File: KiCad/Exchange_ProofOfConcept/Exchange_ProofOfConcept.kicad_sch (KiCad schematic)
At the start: 25 parts, among them J1 Conn_02x03_Odd_Even, J2 Conn_02x03_Odd_Even, J3 Conn_01x04, J7 Screw_Terminal_01x02, J9 Screw_Terminal_01x08, U1 MCP23017, U2 MCP23017, U3 MT8816

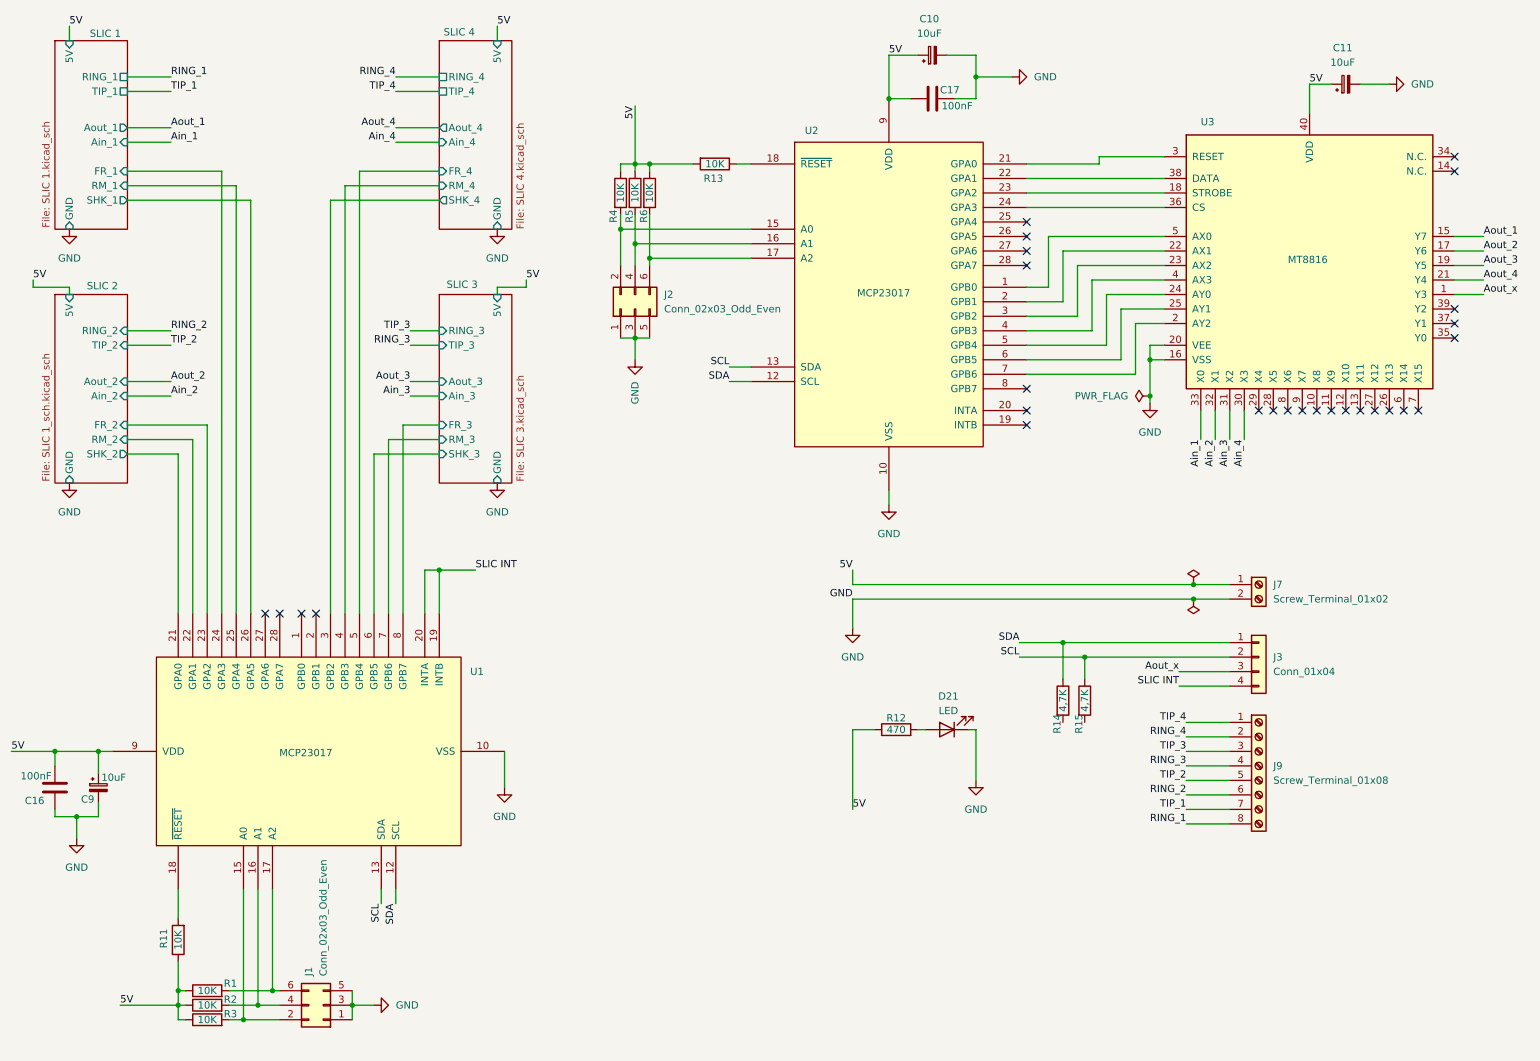
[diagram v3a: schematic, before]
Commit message: deleted:    KiCad/Exchange_ProofOfConcept/Exchange_ProofOfConcept-backups/Exchange_ProofOfConcept-2024-09-22_005800.zip 	deleted:    KiCad/Exchange_ProofOfConcept/Exchange_ProofOfConcept-backups/Exchange_ProofOfConcept-2024-09-22_010415.zip 	deleted:    KiCad/Exchange_ProofOfConcept/Exchange_ProofOfConcept-backups/Exchange_ProofOfConcept-2024-09-22_093037.zip 	deleted:    KiCad/Exchange_ProofOfConcept/Exchange_ProofOfConcept-backups/Exchange_ProofOfConcept-2024-09-22_093847.zip 	deleted:    KiCad/Exchange_ProofOfConcept/Exchange_ProofOfConcept-backups/Exchange_ProofOfConcept-2024-09-22_094927.zip 	deleted:    KiCad/Exchange_ProofOfConcept/Exchange_ProofOfConcept-backups/Exchange_ProofOfConcept-2024-10-02_184119.zip 	deleted:    KiCad/Exchange_ProofOfConcept/Exchange_ProofOfConcept-backups/Exchange_ProofOfConcept-2024-10-06_223658.zip 	new file:   KiCad/Exchange_ProofOfConcept/Exchange_ProofOfConcept-backups/Exchange_ProofOfConcept-2024-11-20_223020.zip 	new file:   KiCad/Exchange_ProofOfConcept/Exchange_ProofOfConcept-backups/Exchange_ProofOfConcept-2024-11-20_223933.zip 	new file:   KiCad/Exchange_ProofOfConcept/Exchange_ProofOfConcept-backups/Exchange_ProofOfConcept-2024-11-20_224852.zip 	new file:   KiCad/Exchange_ProofOfConcept/Exchange_ProofOfConcept-backups/Exchange_ProofOfConcept-2024-11-20_230009.zip 	new file:   KiCad/Exchange_ProofOfConcept/Exchange_ProofOfConcept-backups/Exchange_ProofOfConcept-2024-11-20_231023.zip 	new file:   KiCad/Exchange_ProofOfConcept/Exchange_ProofOfConcept-backups/Exchange_ProofOfConcept-2024-11-20_231736.zip 	modified:   KiCad/Exchange_ProofOfConcept/Exchange_ProofOfConcept.kicad_pcb 	modified:   KiCad/Exchange_ProofOfConcept/Exchange_ProofOfConcept.kicad_prl 	modified:   KiCad/Exchange_ProofOfConcept/Exchange_ProofOfConcept.kicad_pro 	modified:   KiCad/Exchange_ProofOfConcept/Exchange_ProofOfConcept.kicad_sch 	modified:   KiCad/Exchange_ProofOfConcept/SLIC 1.kicad_sch 	modified:   KiCad/Exchange_ProofOfConcept/SLIC 1_sch.kicad_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
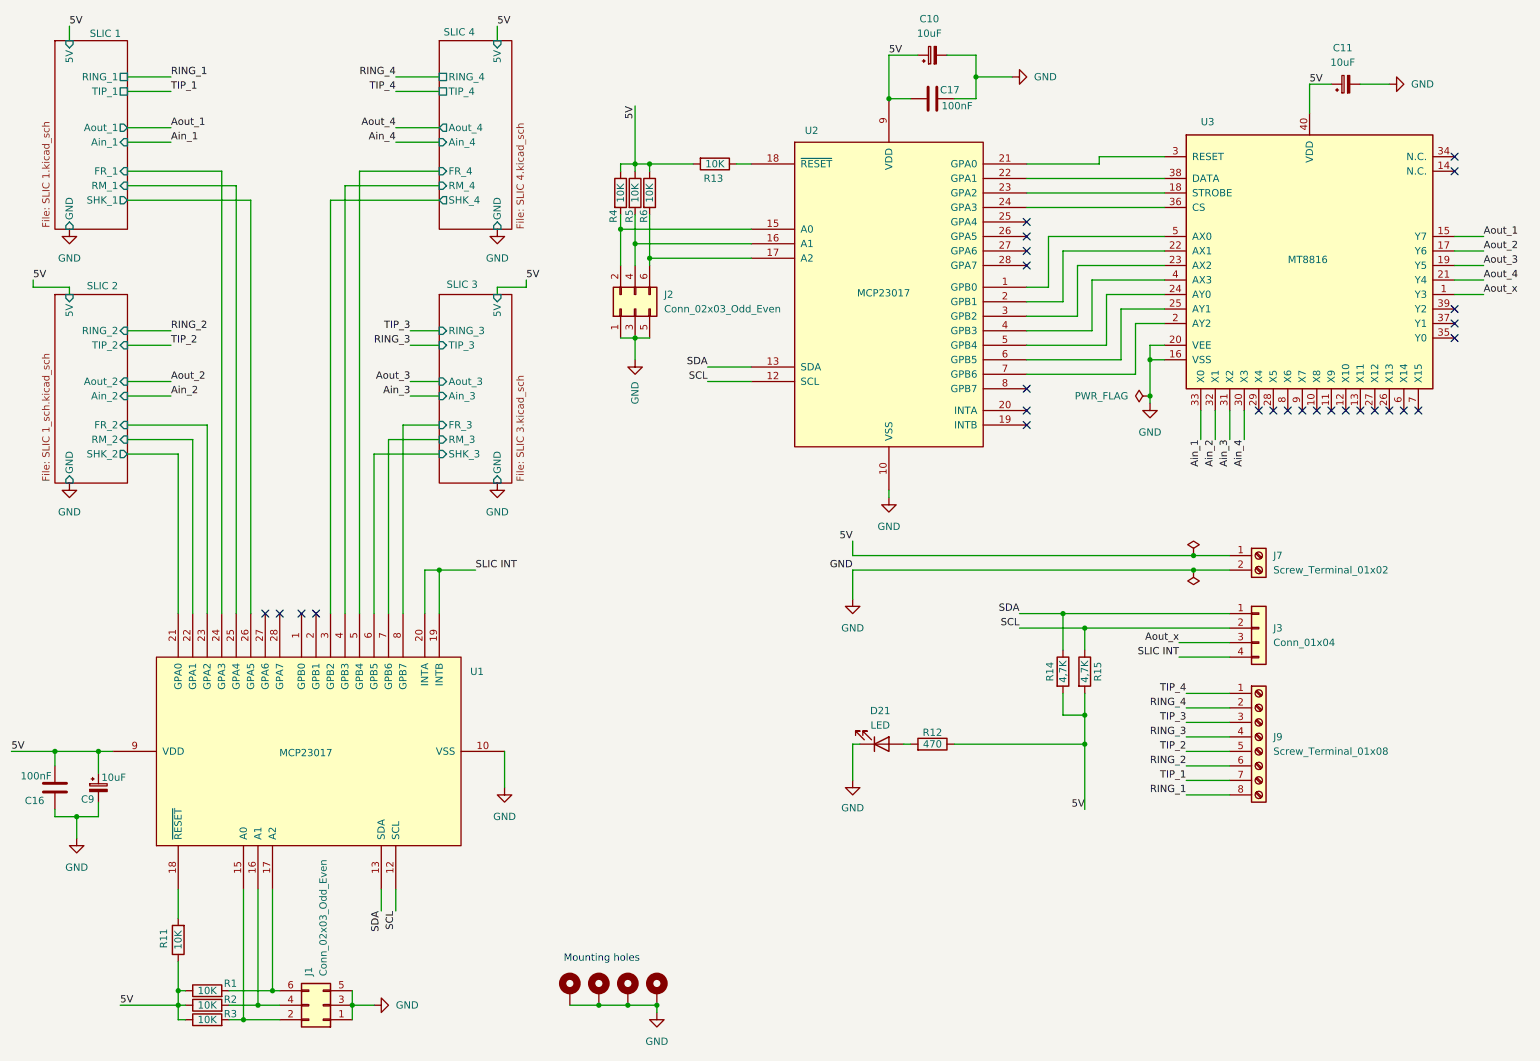
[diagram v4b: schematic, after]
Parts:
- added H1, H2, H3, H4: MountingHole_Pad, MountingHole:MountingHole_3.2mm_M3_Pad_Via, symbol Mechanical:MountingHole_Pad
- R1, R11, R12, R13, R14, R15, R2, R3, R4, R5, R6: footprint Resistor_THT:R_Axial_DIN0207_L6.3mm_D2.5mm_P7.62mm_Horizontal -> Resistor_THT:R_Axial_DIN0207_L6.3mm_D2.5mm_P2.54mm_Vertical
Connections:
- net 5V: now also R14.2, R15.2
- net GND: now also H1.1, H2.1, H3.1, H4.1
- net SCL: now also U1.12 (SCL), U2.12 (SCL); no longer U1.13 (SDA), U2.13 (SDA)
- net SDA: now also U1.13 (SDA), U2.13 (SDA); no longer U1.12 (SCL), U2.12 (SCL)
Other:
- note added: "Mounting holes"
- moved on the sheet: D21, J3, J7, J9, R12, R14, R15
